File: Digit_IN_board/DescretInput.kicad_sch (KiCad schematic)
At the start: 37 parts, among them J4 DS1013-01-10RSiB-B (1)

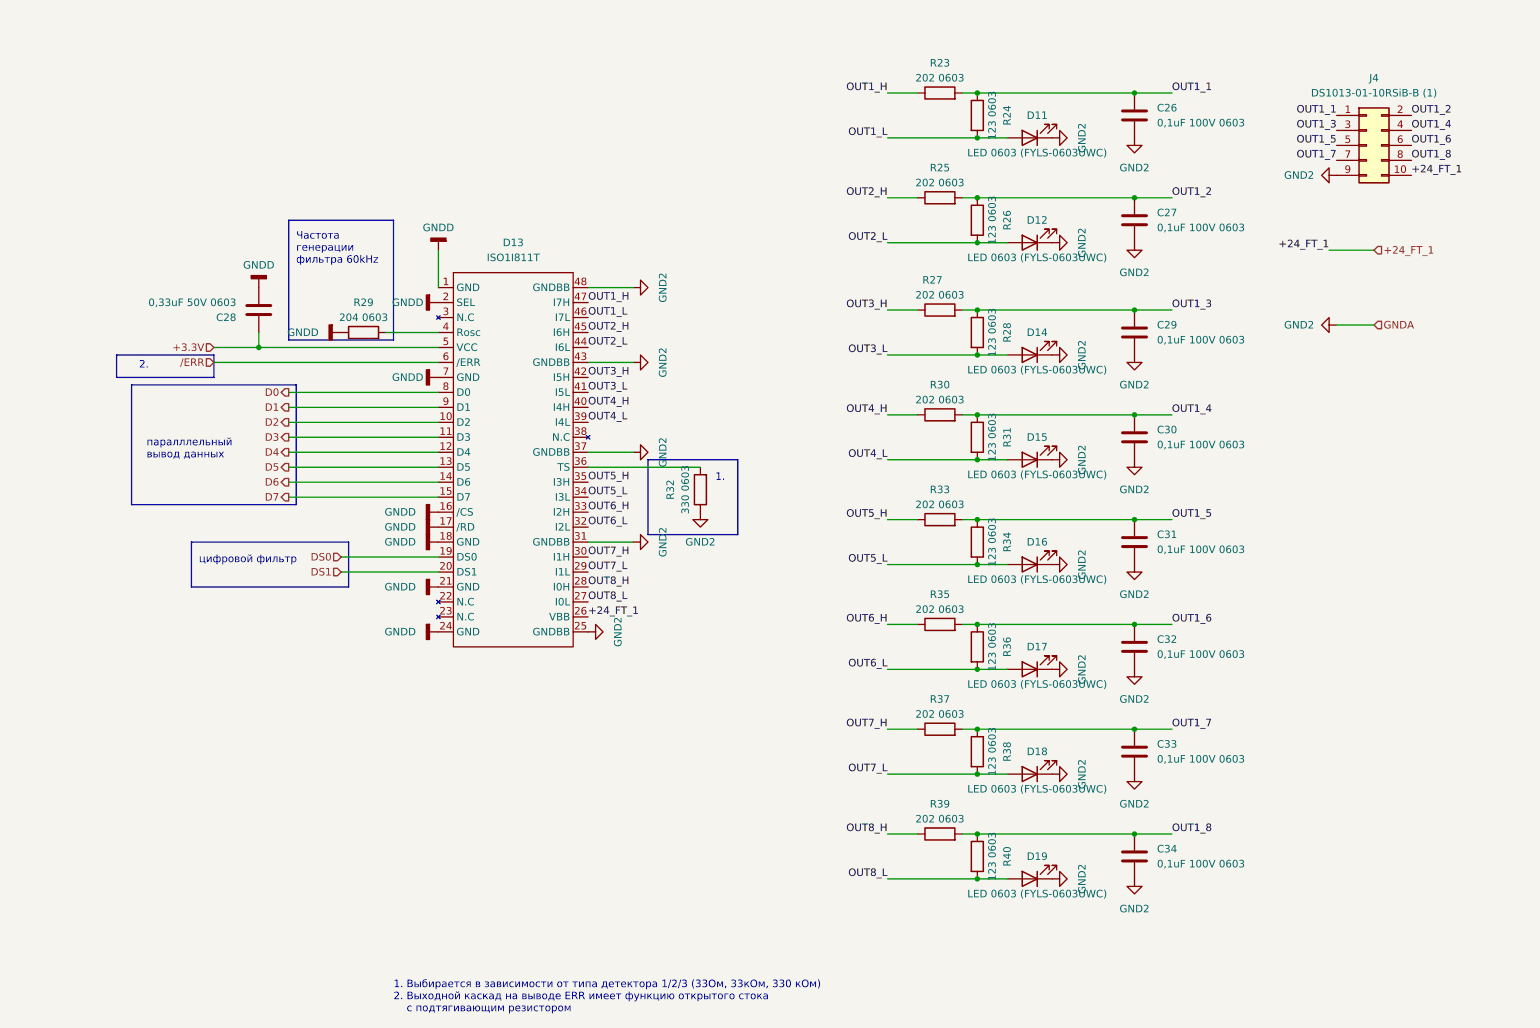
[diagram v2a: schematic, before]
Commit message: DIgit_IN renew schems
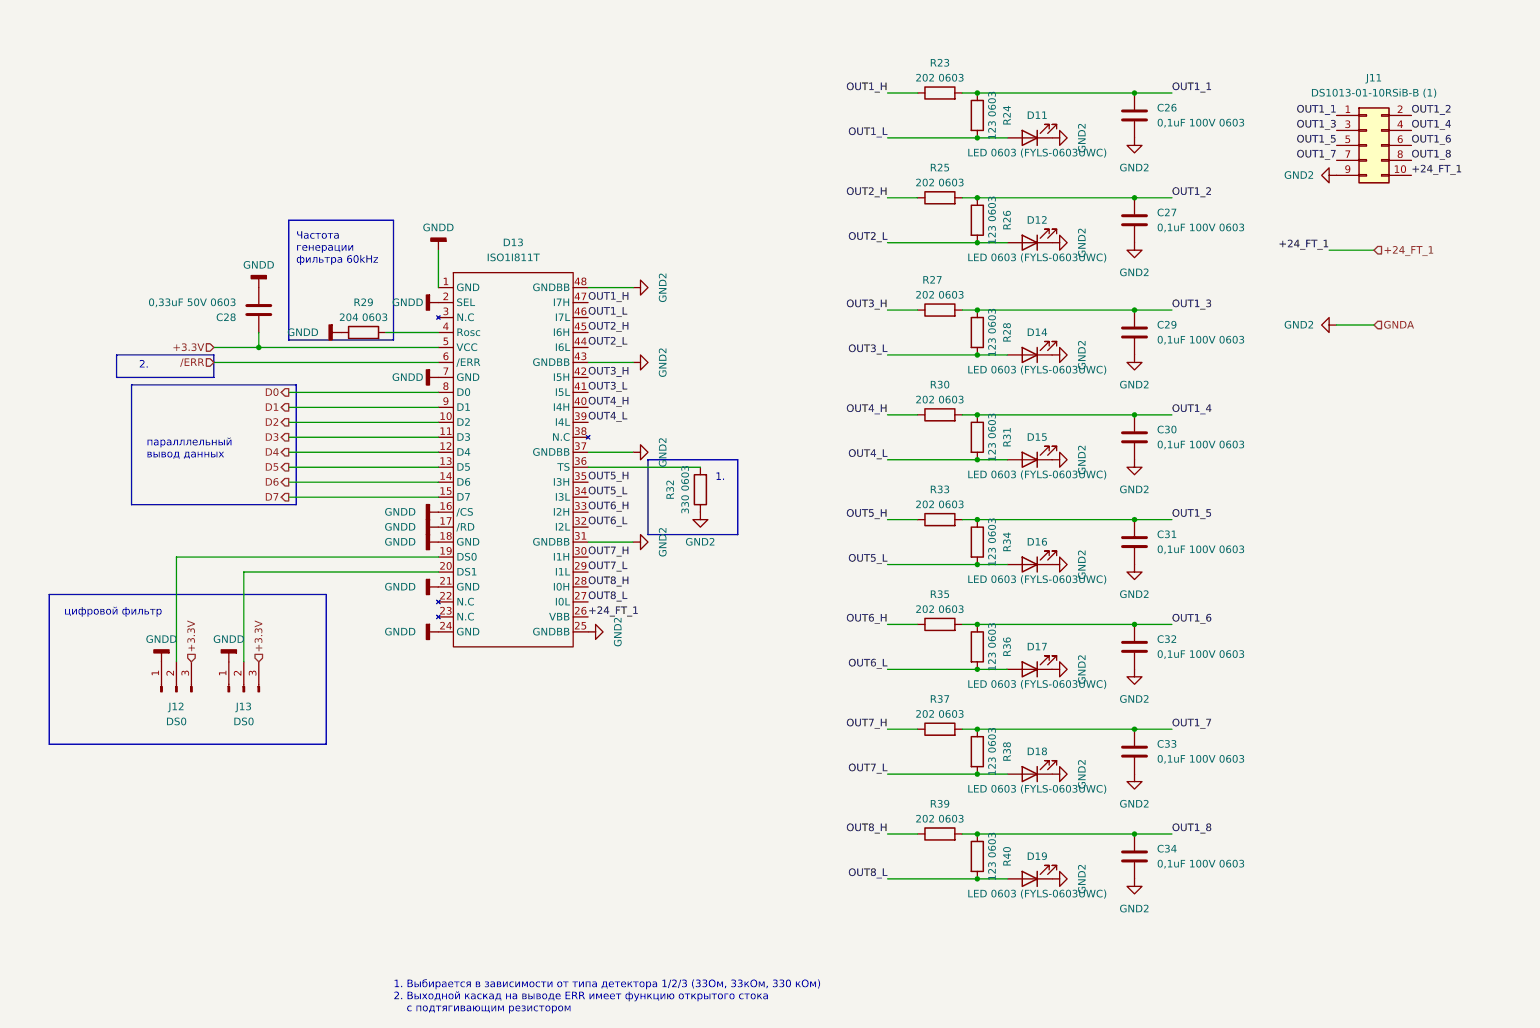
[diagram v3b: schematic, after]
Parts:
- added J12, J13: DS0, Connector_PinHeader_2.54mm:PinHeader_1x03_P2.54mm_Vertical, symbol Connector:Conn_01x03_Pin
- renumbered J4 to J11
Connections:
- net +3.3V: now also J12.3 (Pin_3), J13.3 (Pin_3)
- net GNDD: now also J12.1 (Pin_1), J13.1 (Pin_1)
- net DS0: no longer names the net of D13.19 (DS0)
- net DS0: now also J12.2 (Pin_2)
- net DS1: no longer names the net of D13.20 (DS1)
- net DS1: now also J13.2 (Pin_2)
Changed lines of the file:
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@@
-    (stroke (width 0) (type default))
-  )
-  (wire (pts (xy 85.09 101.6) (xy 101.6 101.6))
     (stroke (width 0) (type default))
   )
@@
     (stroke (width 0) (type default))
   )
+  (wire (pts (xy 57.15 101.6) (xy 101.6 101.6))
+    (stroke (width 0) (type default))
+  )
+  (wire (pts (xy 68.58 119.38) (xy 68.58 104.14))
+    (stroke (width 0) (type default))
+  )
   (wire (pts (xy 63.5 68.58) (xy 101.6 68.58))
     (stroke (width 0) (type default))
@@
     (stroke (width 0) (type default))
   )
-  (wire (pts (xy 85.09 104.14) (xy 101.6 104.14))
-    (stroke (width 0) (type default))
-  )
   (wire (pts (xy 177.8 48.26) (xy 193.04 48.26))
     (stroke (width 0) (type default))
@@
     (stroke (width 0) (type default))
   )
+  (wire (pts (xy 57.15 101.6) (xy 57.15 119.38))
+    (stroke (width 0) (type default))
+  )
   (wire (pts (xy 190.5 40.64) (xy 193.04 40.64))
     (stroke (width 0) (type default))
@@
     (stroke (width 0) (type default))
   )
+  (wire (pts (xy 68.58 104.14) (xy 101.6 104.14))
+    (stroke (width 0) (type default))
+  )
   (wire (pts (xy 219.71 95.25) (xy 226.06 95.25))
     (stroke (width 0) (type default))
@@
     (fill (type none))
   )
-  (rectangle (start 59.69 99.06) (end 86.36 106.68)
+  (rectangle (start 35.56 107.95) (end 82.55 133.35)
     (stroke (width 0) (type default))
     (fill (type none))
@@
     (effects (font (size 1.27 1.27)) (justify left bottom))
   )
-  (text "цифровой фильтр" (at 60.96 102.87 0)
+  (text "цифровой фильтр" (at 38.1 111.76 0)
     (effects (font (size 1.27 1.27)) (justify left bottom))
   )
@@
     (effects (font (size 1.27 1.27)) (justify left bottom))
   )
+  (hierarchical_label "+3.3V" (shape input) (at 59.69 119.38 90) (fields_autoplaced)
+    (effects (font (size 1.27 1.27)) (justify left))
+  )
   (hierarchical_label "D4" (shape output) (at 76.2 83.82 180) (fields_autoplaced)
     (effects (font (size 1.27 1.27)) (justify right))
@@
     (effects (font (size 1.27 1.27)) (justify right))
   )
-  (hierarchical_label "DS1" (shape input) (at 85.09 104.14 180) (fields_autoplaced)
-    (effects (font (size 1.27 1.27)) (justify right))
-  )
   (hierarchical_label "D6" (shape output) (at 76.2 88.9 180) (fields_autoplaced)
     (effects (font (size 1.27 1.27)) (justify right))
@@
     (effects (font (size 1.27 1.27)) (justify right))
   )
-  (hierarchical_label "DS0" (shape input) (at 85.09 101.6 180) (fields_autoplaced)
-    (effects (font (size 1.27 1.27)) (justify right))
+  (hierarchical_label "+3.3V" (shape input) (at 71.12 119.38 90) (fields_autoplaced)
+    (effects (font (size 1.27 1.27)) (justify left))
   )
   (hierarchical_label "{slash}ERR" (shape input) (at 63.5 68.58 180) (fields_autoplaced)
@@
   (symbol (lib_id "Connector_Generic:Conn_02x05_Odd_Even") (at 259.08 31.75 0) (unit 1)
     (in_bom yes) (on_board yes) (dnp no) (fields_autoplaced)
-    (property "Reference" "J4" (at 260.35 20.32 0)
+    (property "Reference" "J11" (at 260.35 20.32 0)
       (effects (font (size 1.27 1.27)))
     )
@@
         (path "/7f8f7dc9-8c50-44ed-985c-35a6d8c67be0/f27e9b73-e584-45db-95e6-e9bb2b701b19"
           (reference "J11") (unit 1)
+        )
+      )
+    )
+  )
+  (symbol (lib_id "power:GNDD") (at 54.61 119.38 180) (unit 1)
+    (in_bom yes) (on_board yes) (dnp no) (fields_autoplaced)
+    (property "Reference" "#PWR0130" (at 54.61 113.03 0)
+      (effects (font (size 1.27 1.27)) hide)
+    )
+    (property "Value" "GNDD" (at 54.61 115.57 0)
+      (effects (font (size 1.27 1.27)))
+    )
+    (property "Footprint" "" (at 54.61 119.38 0)
+      (effects (font (size 1.27 1.27)) hide)
+    )
+    (property "Datasheet" "" (at 54.61 119.38 0)
+      (effects (font (size 1.27 1.27)) hide)
+    )
+    (pin "1")
+    (instances
+      (project "Плата дискретных входов"
+        (path "/7f8f7dc9-8c50-44ed-985c-35a6d8c67be0/f27e9b73-e584-45db-95e6-e9bb2b701b19"
+          (reference "#PWR0130") (unit 1)
         )
       )
@@
     )
   )
+  (symbol (lib_id "Connector:Conn_01x03_Pin") (at 57.15 124.46 90) (unit 1)
+    (in_bom yes) (on_board yes) (dnp no) (fields_autoplaced)
+    (property "Reference" "J12" (at 57.15 127 90)
+      (effects (font (size 1.27 1.27)))
+    )
+    (property "Value" "DS0" (at 57.15 129.54 90)
+      (effects (font (size 1.27 1.27)))
+    )
+    (property "Footprint" "Connector_PinHeader_2.54mm:PinHeader_1x03_P2.54mm_Vertical" (at 57.15 124.46 0)
+      (effects (font (size 1.27 1.27)) hide)
+    )
+    (property "Datasheet" "~" (at 57.15 124.46 0)
+      (effects (font (size 1.27 1.27)) hide)
+    )
+    (pin "1")
+    (pin "3")
+    (pin "2")
+    (instances
+      (project "Плата дискретных входов"
+        (path "/7f8f7dc9-8c50-44ed-985c-35a6d8c67be0/f27e9b73-e584-45db-95e6-e9bb2b701b19"
+          (reference "J12") (unit 1)
+        )
+      )
+    )
+  )
   (symbol (lib_id "Device:LED") (at 201.93 156.21 180) (unit 1)
     (in_bom yes) (on_board yes) (dnp no)
@@
     )
   )
+  (symbol (lib_id "Connector:Conn_01x03_Pin") (at 68.58 124.46 90) (unit 1)
+    (in_bom yes) (on_board yes) (dnp no) (fields_autoplaced)
+    (property "Reference" "J13" (at 68.58 127 90)
+      (effects (font (size 1.27 1.27)))
+    )
+    (property "Value" "DS0" (at 68.58 129.54 90)
+      (effects (font (size 1.27 1.27)))
+    )
+    (property "Footprint" "Connector_PinHeader_2.54mm:PinHeader_1x03_P2.54mm_Vertical" (at 68.58 124.46 0)
+      (effects (font (size 1.27 1.27)) hide)
+    )
+    (property "Datasheet" "~" (at 68.58 124.46 0)
+      (effects (font (size 1.27 1.27)) hide)
+    )
+    (pin "1")
+    (pin "3")
+    (pin "2")
+    (instances
+      (project "Плата дискретных входов"
+        (path "/7f8f7dc9-8c50-44ed-985c-35a6d8c67be0/f27e9b73-e584-45db-95e6-e9bb2b701b19"
+          (reference "J13") (unit 1)
+        )
+      )
+    )
+  )
   (symbol (lib_id "Device:LED") (at 201.93 120.65 180) (unit 1)
     (in_bom yes) (on_board yes) (dnp no)
@@
         )
       )
+    )
+  )
+  (symbol (lib_id "power:GNDD") (at 66.04 119.38 180) (unit 1)
+    (in_bom yes) (on_board yes) (dnp no) (fields_autoplaced)
+    (property "Reference" "#PWR0131" (at 66.04 113.03 0)
+      (effects (font (size 1.27 1.27)) hide)
+    )
+    (property "Value" "GNDD" (at 66.04 115.57 0)
+      (effects (font (size 1.27 1.27)))
+    )
+    (property "Footprint" "" (at 66.04 119.38 0)
+      (effects (font (size 1.27 1.27)) hide)
+    )
+    (property "Datasheet" "" (at 66.04 119.38 0)
+      (effects (font (size 1.27 1.27)) hide)
+    )
+    (pin "1")
+    (instances
+      (project "Плата дискретных входов"
+        (path "/7f8f7dc9-8c50-44ed-985c-35a6d8c67be0/f27e9b73-e584-45db-95e6-e9bb2b701b19"
+          (reference "#PWR0131") (unit 1)
+        )
+      )

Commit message: Discret IN_OUT schems and PCB
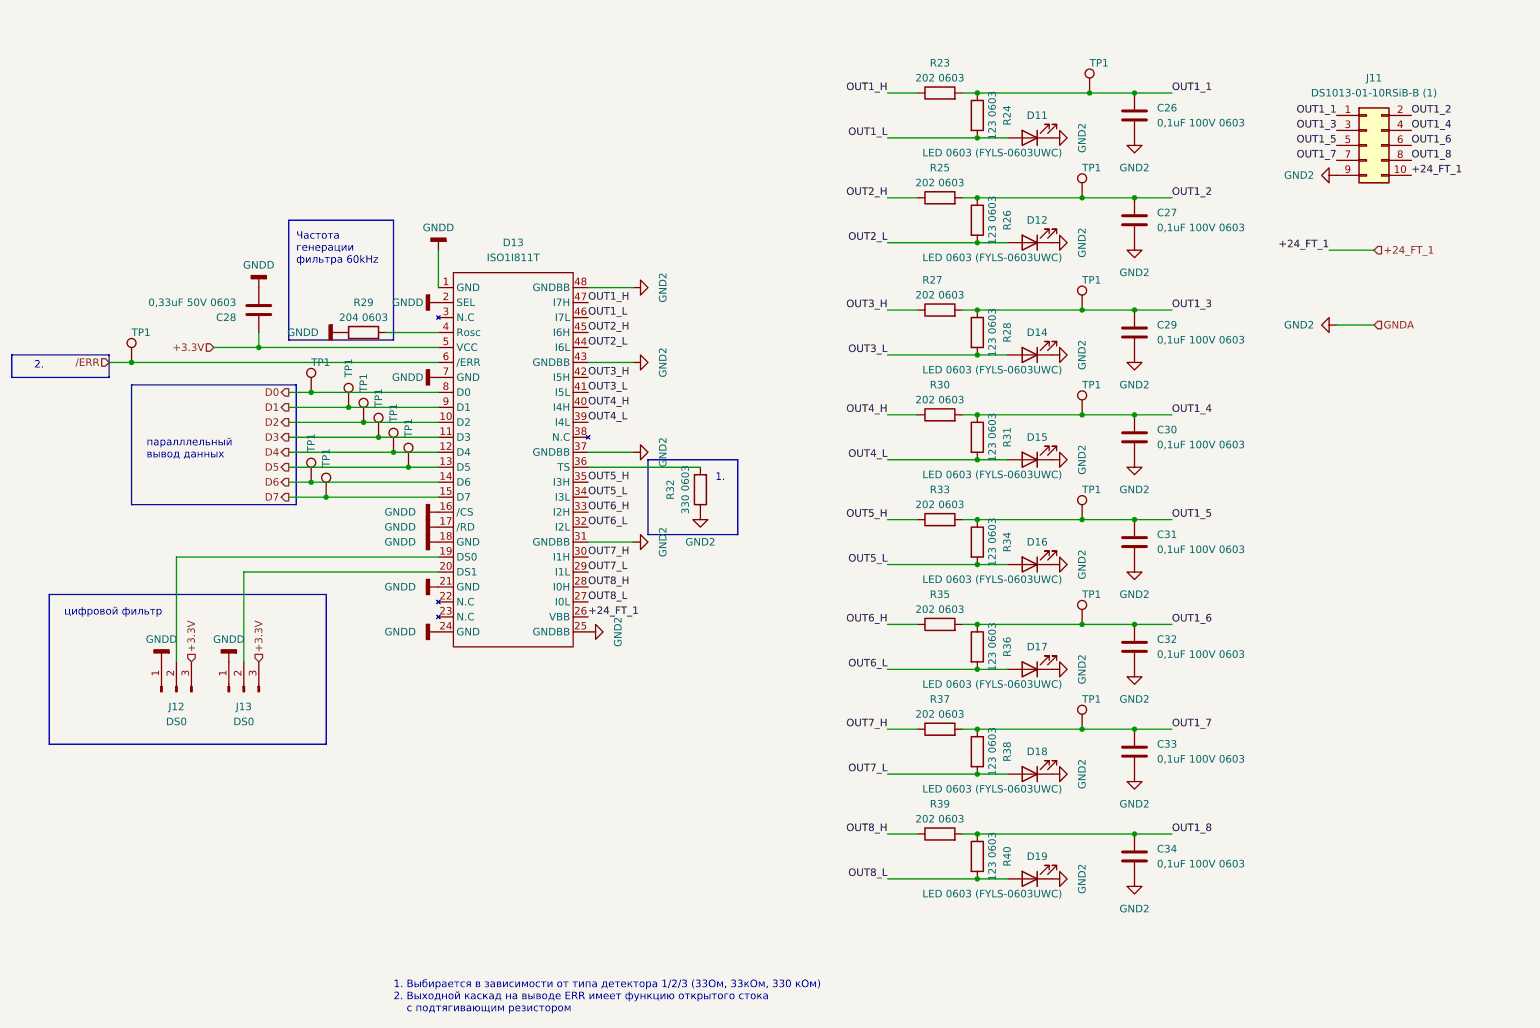
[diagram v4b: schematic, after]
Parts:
- added TP1 (x16): ~, PCM_4ms_TestPoint:TestPoint_D1, symbol Connector:TestPoint
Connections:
- net D0: now also TP1.1
- net D1: now also TP1.1
- net D2: now also TP1.1
- net D3: now also TP1.1
- net D4: now also TP1.1
- net D5: now also TP1.1
- net D6: now also TP1.1
- net D7: now also TP1.1
- net OUT1_1: now also TP1.1
- net OUT1_2: now also TP1.1
- net OUT1_3: now also TP1.1
- net OUT1_4: now also TP1.1
- net OUT1_5: now also TP1.1
- net OUT1_6: now also TP1.1
- net OUT1_7: now also TP1.1
- net /ERR: now also TP1.1

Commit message: renew all schems and pcb for production
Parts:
- R23, R25, R27, R30, R33, R35, R37, R39: value 202 0603 -> 0603-2 кОм±5%-0,062 Вт
- R24, R26, R28, R31, R34, R36, R38, R40: value 123 0603 -> 0603-12 кОм±5%-0,062 Вт
- R29: value 204 0603 -> 0603-200 кОм±5%-0,062 Вт
- R32: value 330 0603 -> 0603-33 Ом±5%-0,062 Вт
- TP1: now left out of the parts list

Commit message: RENEW ALL BOARDS
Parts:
- C26, C27, C29, C30, C31, C32, C33, C34: footprint Capacitor_SMD:C_0603_1608Metric_Pad1.08x0.95mm_HandSolder -> PCM_Capacitor_SMD_AKL:C_0603_1608Metric_Pad1.08x0.95mm_HandSolder
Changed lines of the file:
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@@
       (effects (font (size 1.27 1.27)) (justify left))
     )
-    (property "Footprint" "Capacitor_SMD:C_0603_1608Metric_Pad1.08x0.95mm_HandSolder" (at 220.6752 120.65 0)
+    (property "Footprint" "PCM_Capacitor_SMD_AKL:C_0603_1608Metric_Pad1.08x0.95mm_HandSolder" (at 220.6752 120.65 0)
       (effects (font (size 1.27 1.27)) hide)
     )
@@
       (effects (font (size 1.27 1.27)) (justify left))
     )
-    (property "Footprint" "Capacitor_SMD:C_0603_1608Metric_Pad1.08x0.95mm_HandSolder" (at 220.6752 138.43 0)
+    (property "Footprint" "PCM_Capacitor_SMD_AKL:C_0603_1608Metric_Pad1.08x0.95mm_HandSolder" (at 220.6752 138.43 0)
       (effects (font (size 1.27 1.27)) hide)
     )
@@
       (effects (font (size 1.27 1.27)) (justify left))
     )
-    (property "Footprint" "Capacitor_SMD:C_0603_1608Metric_Pad1.08x0.95mm_HandSolder" (at 220.6752 67.31 0)
+    (property "Footprint" "PCM_Capacitor_SMD_AKL:C_0603_1608Metric_Pad1.08x0.95mm_HandSolder" (at 220.6752 67.31 0)
       (effects (font (size 1.27 1.27)) hide)
     )
@@
       (effects (font (size 1.27 1.27)) (justify left))
     )
-    (property "Footprint" "Capacitor_SMD:C_0603_1608Metric_Pad1.08x0.95mm_HandSolder" (at 220.6752 102.87 0)
+    (property "Footprint" "PCM_Capacitor_SMD_AKL:C_0603_1608Metric_Pad1.08x0.95mm_HandSolder" (at 220.6752 102.87 0)
       (effects (font (size 1.27 1.27)) hide)
     )
@@
       (effects (font (size 1.27 1.27)) (justify left))
     )
-    (property "Footprint" "Capacitor_SMD:C_0603_1608Metric_Pad1.08x0.95mm_HandSolder" (at 220.6752 156.21 0)
+    (property "Footprint" "PCM_Capacitor_SMD_AKL:C_0603_1608Metric_Pad1.08x0.95mm_HandSolder" (at 220.6752 156.21 0)
       (effects (font (size 1.27 1.27)) hide)
     )
@@
       (effects (font (size 1.27 1.27)) (justify left))
     )
-    (property "Footprint" "Capacitor_SMD:C_0603_1608Metric_Pad1.08x0.95mm_HandSolder" (at 220.6752 48.26 0)
+    (property "Footprint" "PCM_Capacitor_SMD_AKL:C_0603_1608Metric_Pad1.08x0.95mm_HandSolder" (at 220.6752 48.26 0)
       (effects (font (size 1.27 1.27)) hide)
     )
@@
       (effects (font (size 1.27 1.27)) (justify left))
     )
-    (property "Footprint" "Capacitor_SMD:C_0603_1608Metric_Pad1.08x0.95mm_HandSolder" (at 220.6752 85.09 0)
+    (property "Footprint" "PCM_Capacitor_SMD_AKL:C_0603_1608Metric_Pad1.08x0.95mm_HandSolder" (at 220.6752 85.09 0)
       (effects (font (size 1.27 1.27)) hide)
     )
@@
       (effects (font (size 1.27 1.27)) (justify left))
     )
-    (property "Footprint" "Capacitor_SMD:C_0603_1608Metric_Pad1.08x0.95mm_HandSolder" (at 220.6752 30.48 0)
-      (effects (font (size 1.27 1.27)) hide)
-    )
+    (property "Footprint" "PCM_Capacitor_SMD_AKL:C_0603_1608Metric_Pad1.08x0.95mm_HandSolder" (at 220.6752 30.48 0)
+      (effects (font (size 1.27 1.27)) hide)
+    )
